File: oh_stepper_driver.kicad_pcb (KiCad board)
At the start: 2 copper layers, 61 x 43.2 mm, 26 parts, among them P1 CONN_01X04, Q1 CSD18531Q5A, Q2 CSD18531Q5A, Q3 CSD18531Q5A, Q4 CSD18531Q5A, Q5 CSD18531Q5A, Q6 CSD18531Q5A, Q7 CSD18531Q5A, Q8 CSD18531Q5A, U1 DRV8711

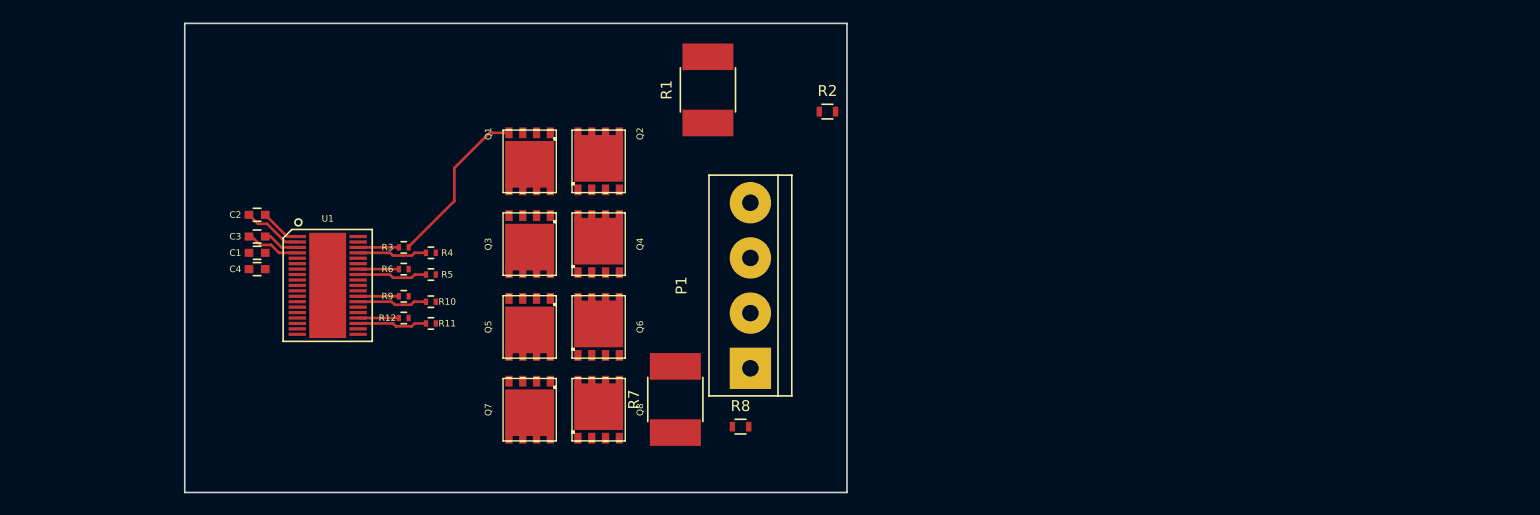
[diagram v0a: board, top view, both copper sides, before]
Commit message: FETs sheet added
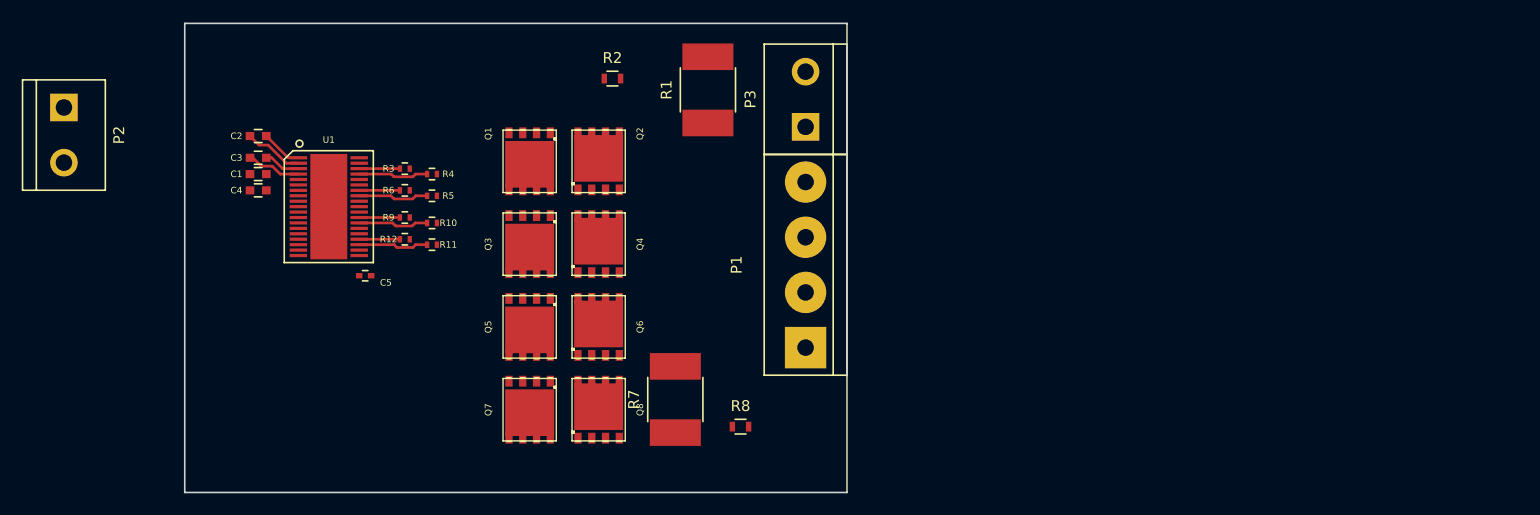
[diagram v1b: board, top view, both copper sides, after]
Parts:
- added C5: 1000pF, Capacitors_SMD:C_0402, F.Cu at (133.4, 79.1)
- added P2: CONN_01X02, Connectors:bornier2, F.Cu at (105.7, 66.2)
- added P3: CONN_01X02, Connectors:bornier2, F.Cu at (174.0, 62.9)
- moved R2 20.0 mm to (156.2, 61.0)
- moved C1 7.25 mm to (123.6, 69.8)
- moved C2 7.25 mm to (123.6, 68.2)
- moved C3 7.25 mm to (123.6, 66.2)
- moved C4 7.25 mm to (123.6, 71.2)
- moved R10 7.25 mm to (139.6, 74.2)
- moved R11 7.25 mm to (139.6, 76.2)
- moved R12 7.25 mm to (137.1, 75.8)
- moved R3 7.25 mm to (137.1, 69.2)
- moved R4 7.25 mm to (139.6, 69.8)
- moved R5 7.25 mm to (139.6, 71.8)
- moved R6 7.25 mm to (137.1, 71.2)
- moved R9 7.25 mm to (137.1, 73.8)
- moved U1 7.25 mm to (130.1, 72.8)
- moved P1 5.43 mm to (174.0, 78.1)
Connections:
- U1 pad 20: (no net) -> Net-(C5-Pad1)
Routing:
- net Net-(Q1-PadG): track 15.4 -> 0.06 mm

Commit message: adding capacitors to the PCB
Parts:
- added C7: 10uF, Capacitors_SMD:C_2220, F.Cu at (194.0, 60.8)
- added C8: 0.1uF, Capacitors_SMD:C_0603, F.Cu at (200.2, 58.7)
- added C9: 0.01uF, Capacitors_SMD:C_0603, F.Cu at (205.3, 58.7)
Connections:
- U1 pad 10: (no net) -> /STEP_AIN1
- U1 pad 11: (no net) -> /DIR_AIN2
- U1 pad 12: (no net) -> /BIN1
- U1 pad 13: (no net) -> /BIN2
- U1 pad 14: (no net) -> /SCLK
- U1 pad 15: (no net) -> /SDATI
- U1 pad 16: (no net) -> /SCS
- U1 pad 17: (no net) -> /SDATAO
- U1 pad 18: (no net) -> /FAULTn
- U1 pad 19: (no net) -> /STALLn
- U1 pad 8: (no net) -> /SLEEPn
- U1 pad 9: (no net) -> /RESET
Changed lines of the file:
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@@
 (kicad_pcb (version 20160815) (host pcbnew no-vcs-found-7399~56~ubuntu16.04.1)
   (general
-    (links 109)
-    (no_connects 97)
+    (links 113)
+    (no_connects 99)
     (area 116.764999 55.804999 177.875001 99.135001)
     (thickness 1.6)
@@
     (tracks 40)
     (zones 0)
-    (modules 29)
-    (nets 33)
+    (modules 32)
+    (nets 47)
   )
   (page A4)
@@
   (net 31 /AISENN)
   (net 32 "Net-(C5-Pad1)")
+  (net 33 /STALLn)
+  (net 34 /FAULTn)
+  (net 35 /SDATAO)
+  (net 36 /SCS)
+  (net 37 /SDATI)
+  (net 38 /SCLK)
+  (net 39 /BIN2)
+  (net 40 /BIN1)
+  (net 41 /DIR_AIN2)
+  (net 42 /STEP_AIN1)
+  (net 43 /RESET)
+  (net 44 /SLEEPn)
+  (net 45 "Net-(C7-Pad2)")
+  (net 46 "Net-(C7-Pad1)")
   (net_class Default "This is the default net class."
     (clearance 0.2)
@@
     (add_net /B2HS)
     (add_net /B2LS)
+    (add_net /BIN1)
+    (add_net /BIN2)
     (add_net /BISENN)
     (add_net /BISENP)
     (add_net /BOUT1)
     (add_net /BOUT2)
+    (add_net /DIR_AIN2)
+    (add_net /FAULTn)
+    (add_net /RESET)
+    (add_net /SCLK)
+    (add_net /SCS)
+    (add_net /SDATAO)
+    (add_net /SDATI)
+    (add_net /SLEEPn)
+    (add_net /STALLn)
+    (add_net /STEP_AIN1)
     (add_net GND)
     (add_net "Net-(C1-Pad1)")
@@
     (add_net "Net-(C4-Pad1)")
     (add_net "Net-(C5-Pad1)")
+    (add_net "Net-(C7-Pad1)")
+    (add_net "Net-(C7-Pad2)")
     (add_net "Net-(Q1-PadG)")
     (add_net "Net-(Q2-PadG)")
@@
     (add_net "Net-(Q8-PadG)")
     (add_net VM)
+  )
+  (module Capacitors_SMD:C_0603 (layer F.Cu)
+    (at 205.325119 58.662499)
+    (descr "Capacitor SMD 0603, reflow soldering, AVX (see smccp.pdf)")
+    (tags "capacitor 0603")
+    (attr smd)
+    (fp_text reference C9 (at 0 -1.9) (layer F.SilkS)
+      (effects (font (size 0.6 0.6) (thickness 0.15)))
+    )
+    (fp_text value 0.01uF (at 0 1.9) (layer F.Fab)
+      (effects (font (size 1 1) (thickness 0.15)))
+    )
+    (fp_line (start -0.8 0.4) (end -0.8 -0.4) (layer F.Fab) (width 0.15))
+    (fp_line (start 0.8 0.4) (end -0.8 0.4) (layer F.Fab) (width 0.15))
+    (fp_line (start 0.8 -0.4) (end 0.8 0.4) (layer F.Fab) (width 0.15))
+    (fp_line (start -0.8 -0.4) (end 0.8 -0.4) (layer F.Fab) (width 0.15))
+    (fp_line (start -1.45 -0.75) (end 1.45 -0.75) (layer F.CrtYd) (width 0.05))
+    (fp_line (start -1.45 0.75) (end 1.45 0.75) (layer F.CrtYd) (width 0.05))
+    (fp_line (start -1.45 -0.75) (end -1.45 0.75) (layer F.CrtYd) (width 0.05))
+    (fp_line (start 1.45 -0.75) (end 1.45 0.75) (layer F.CrtYd) (width 0.05))
+    (fp_line (start -0.35 -0.6) (end 0.35 -0.6) (layer F.SilkS) (width 0.15))
+    (fp_line (start 0.35 0.6) (end -0.35 0.6) (layer F.SilkS) (width 0.15))
+    (pad 1 smd rect (at -0.75 0) (size 0.8 0.75) (layers F.Cu F.Paste F.Mask)
+      (net 46 "Net-(C7-Pad1)"))
+    (pad 2 smd rect (at 0.75 0) (size 0.8 0.75) (layers F.Cu F.Paste F.Mask)
+      (net 45 "Net-(C7-Pad2)"))
+    (model Capacitors_SMD.3dshapes/C_0603.wrl
+      (at (xyz 0 0 0))
+      (scale (xyz 1 1 1))
+      (rotate (xyz 0 0 0))
+    )
+  )
+  (module Capacitors_SMD:C_0603 (layer F.Cu)
+    (at 200.158928 58.662499)
+    (descr "Capacitor SMD 0603, reflow soldering, AVX (see smccp.pdf)")
+    (tags "capacitor 0603")
+    (attr smd)
+    (fp_text reference C8 (at 0 -1.9) (layer F.SilkS)
+      (effects (font (size 0.6 0.6) (thickness 0.15)))
+    )
+    (fp_text value 0.1uF (at 0 1.9) (layer F.Fab)
+      (effects (font (size 1 1) (thickness 0.15)))
+    )
+    (fp_line (start 0.35 0.6) (end -0.35 0.6) (layer F.SilkS) (width 0.15))
+    (fp_line (start -0.35 -0.6) (end 0.35 -0.6) (layer F.SilkS) (width 0.15))
+    (fp_line (start 1.45 -0.75) (end 1.45 0.75) (layer F.CrtYd) (width 0.05))
+    (fp_line (start -1.45 -0.75) (end -1.45 0.75) (layer F.CrtYd) (width 0.05))
+    (fp_line (start -1.45 0.75) (end 1.45 0.75) (layer F.CrtYd) (width 0.05))
+    (fp_line (start -1.45 -0.75) (end 1.45 -0.75) (layer F.CrtYd) (width 0.05))
+    (fp_line (start -0.8 -0.4) (end 0.8 -0.4) (layer F.Fab) (width 0.15))
+    (fp_line (start 0.8 -0.4) (end 0.8 0.4) (layer F.Fab) (width 0.15))
+    (fp_line (start 0.8 0.4) (end -0.8 0.4) (layer F.Fab) (width 0.15))
+    (fp_line (start -0.8 0.4) (end -0.8 -0.4) (layer F.Fab) (width 0.15))
+    (pad 2 smd rect (at 0.75 0) (size 0.8 0.75) (layers F.Cu F.Paste F.Mask)
+      (net 45 "Net-(C7-Pad2)"))
+    (pad 1 smd rect (at -0.75 0) (size 0.8 0.75) (layers F.Cu F.Paste F.Mask)
+      (net 46 "Net-(C7-Pad1)"))
+    (model Capacitors_SMD.3dshapes/C_0603.wrl
+      (at (xyz 0 0 0))
+      (scale (xyz 1 1 1))
+      (rotate (xyz 0 0 0))
+    )
+  )
+  (module Capacitors_SMD:C_2220 (layer F.Cu)
+    (at 193.987501 60.762499)
+    (descr "Capacitor SMD 2220, reflow soldering, AVX (see smccp.pdf)")
+    (tags "capacitor 2220")
+    (attr smd)
+    (fp_text reference C7 (at 0 -4) (layer F.SilkS)
+      (effects (font (size 0.6 0.6) (thickness 0.15)))
+    )
+    (fp_text value 10uF (at 0 4) (layer F.Fab)
+      (effects (font (size 1 1) (thickness 0.15)))
+    )
+    (fp_line (start -2.3 2.725) (end 2.3 2.725) (layer F.SilkS) (width 0.15))
+    (fp_line (start 2.3 -2.725) (end -2.3 -2.725) (layer F.SilkS) (width 0.15))
+    (fp_line (start 3.6 -2.85) (end 3.6 2.85) (layer F.CrtYd) (width 0.05))
+    (fp_line (start -3.6 -2.85) (end -3.6 2.85) (layer F.CrtYd) (width 0.05))
+    (fp_line (start -3.6 2.85) (end 3.6 2.85) (layer F.CrtYd) (width 0.05))
+    (fp_line (start -3.6 -2.85) (end 3.6 -2.85) (layer F.CrtYd) (width 0.05))
+    (fp_line (start -2.75 -2.5) (end 2.75 -2.5) (layer F.Fab) (width 0.15))
+    (fp_line (start 2.75 -2.5) (end 2.75 2.5) (layer F.Fab) (width 0.15))
+    (fp_line (start 2.75 2.5) (end -2.75 2.5) (layer F.Fab) (width 0.15))
+    (fp_line (start -2.75 2.5) (end -2.75 -2.5) (layer F.Fab) (width 0.15))
+    (pad 2 smd rect (at 2.8 0) (size 1 5) (layers F.Cu F.Paste F.Mask)
+      (net 45 "Net-(C7-Pad2)"))
+    (pad 1 smd rect (at -2.8 0) (size 1 5) (layers F.Cu F.Paste F.Mask)
+      (net 46 "Net-(C7-Pad1)"))
+    (model Capacitors_SMD.3dshapes/C_2220.wrl
+      (at (xyz 0 0 0))
+      (scale (xyz 1 1 1))
+      (rotate (xyz 0 0 0))
+    )
   )
   (module Connectors:bornier2 (layer F.Cu)
@@
     (fp_line (start -5.15 3.3) (end -5.15 -4.1) (layer F.SilkS) (width 0.15))
     (fp_line (start -4.35 4.1) (end -5.15 3.3) (layer F.SilkS) (width 0.15))
-    (pad 19 smd rect (at 4.5 2.8 270) (size 0.3 1.6) (layers F.Cu F.Paste F.Mask))
+    (pad 19 smd rect (at 4.5 2.8 270) (size 0.3 1.6) (layers F.Cu F.Paste F.Mask)
+      (net 33 /STALLn))
     (pad 20 smd rect (at 4.5 -2.8 270) (size 0.3 1.6) (layers F.Cu F.Paste F.Mask)
       (net 32 "Net-(C5-Pad1)"))
-    (pad 18 smd rect (at 4 2.8 270) (size 0.3 1.6) (layers F.Cu F.Paste F.Mask))
+    (pad 18 smd rect (at 4 2.8 270) (size 0.3 1.6) (layers F.Cu F.Paste F.Mask)
+      (net 34 /FAULTn))
     (pad 21 smd rect (at 4 -2.8 270) (size 0.3 1.6) (layers F.Cu F.Paste F.Mask)
       (net 6 /BOUT2))
-    (pad 17 smd rect (at 3.5 2.8 270) (size 0.3 1.6) (layers F.Cu F.Paste F.Mask))
+    (pad 17 smd rect (at 3.5 2.8 270) (size 0.3 1.6) (layers F.Cu F.Paste F.Mask)
+      (net 35 /SDATAO))
     (pad 22 smd rect (at 3.5 -2.8 270) (size 0.3 1.6) (layers F.Cu F.Paste F.Mask)
       (net 28 /B2HS))
-    (pad 16 smd rect (at 3 2.8 270) (size 0.3 1.6) (layers F.Cu F.Paste F.Mask))
+    (pad 16 smd rect (at 3 2.8 270) (size 0.3 1.6) (layers F.Cu F.Paste F.Mask)
+      (net 36 /SCS))
     (pad 23 smd rect (at 3 -2.8 270) (size 0.3 1.6) (layers F.Cu F.Paste F.Mask)
       (net 29 /B2LS))
-    (pad 15 smd rect (at 2.5 2.8 270) (size 0.3 1.6) (layers F.Cu F.Paste F.Mask))
+    (pad 15 smd rect (at 2.5 2.8 270) (size 0.3 1.6) (layers F.Cu F.Paste F.Mask)
+      (net 37 /SDATI))
     (pad 24 smd rect (at 2.5 -2.8 270) (size 0.3 1.6) (layers F.Cu F.Paste F.Mask)
       (net 30 /BISENN))
-    (pad 14 smd rect (at 2 2.8 270) (size 0.3 1.6) (layers F.Cu F.Paste F.Mask))
+    (pad 14 smd rect (at 2 2.8 270) (size 0.3 1.6) (layers F.Cu F.Paste F.Mask)
+      (net 38 /SCLK))
     (pad 25 smd rect (at 2 -2.8 270) (size 0.3 1.6) (layers F.Cu F.Paste F.Mask)
       (net 19 /BISENP))
-    (pad 13 smd rect (at 1.5 2.8 270) (size 0.3 1.6) (layers F.Cu F.Paste F.Mask))
+    (pad 13 smd rect (at 1.5 2.8 270) (size 0.3 1.6) (layers F.Cu F.Paste F.Mask)
+      (net 39 /BIN2))
     (pad 26 smd rect (at 1.5 -2.8 270) (size 0.3 1.6) (layers F.Cu F.Paste F.Mask)
       (net 27 /B1LS))
-    (pad 12 smd rect (at 1 2.8 270) (size 0.3 1.6) (layers F.Cu F.Paste F.Mask))
+    (pad 12 smd rect (at 1 2.8 270) (size 0.3 1.6) (layers F.Cu F.Paste F.Mask)
+      (net 40 /BIN1))
     (pad 27 smd rect (at 1 -2.8 270) (size 0.3 1.6) (layers F.Cu F.Paste F.Mask)
       (net 26 /B1HS))
-    (pad 11 smd rect (at 0.5 2.8 270) (size 0.3 1.6) (layers F.Cu F.Paste F.Mask))
+    (pad 11 smd rect (at 0.5 2.8 270) (size 0.3 1.6) (layers F.Cu F.Paste F.Mask)
+      (net 41 /DIR_AIN2))
     (pad 28 smd rect (at 0.5 -2.8 270) (size 0.3 1.6) (layers F.Cu F.Paste F.Mask)
       (net 5 /BOUT1))
-    (pad 10 smd rect (at 0 2.8 270) (size 0.3 1.6) (layers F.Cu F.Paste F.Mask))
+    (pad 10 smd rect (at 0 2.8 270) (size 0.3 1.6) (layers F.Cu F.Paste F.Mask)
+      (net 42 /STEP_AIN1))
     (pad 29 smd rect (at 0 -2.8 270) (size 0.3 1.6) (layers F.Cu F.Paste F.Mask)
       (net 7 GND))
-    (pad 9 smd rect (at -0.5 2.8 270) (size 0.3 1.6) (layers F.Cu F.Paste F.Mask))
+    (pad 9 smd rect (at -0.5 2.8 270) (size 0.3 1.6) (layers F.Cu F.Paste F.Mask)
+      (net 43 /RESET))
     (pad 30 smd rect (at -0.5 -2.8 270) (size 0.3 1.6) (layers F.Cu F.Paste F.Mask)
       (net 4 /AOUT2))
-    (pad 8 smd rect (at -1 2.8 270) (size 0.3 1.6) (layers F.Cu F.Paste F.Mask))
+    (pad 8 smd rect (at -1 2.8 270) (size 0.3 1.6) (layers F.Cu F.Paste F.Mask)
+      (net 44 /SLEEPn))
     (pad 31 smd rect (at -1 -2.8 270) (size 0.3 1.6) (layers F.Cu F.Paste F.Mask)
       (net 24 /A2HS))

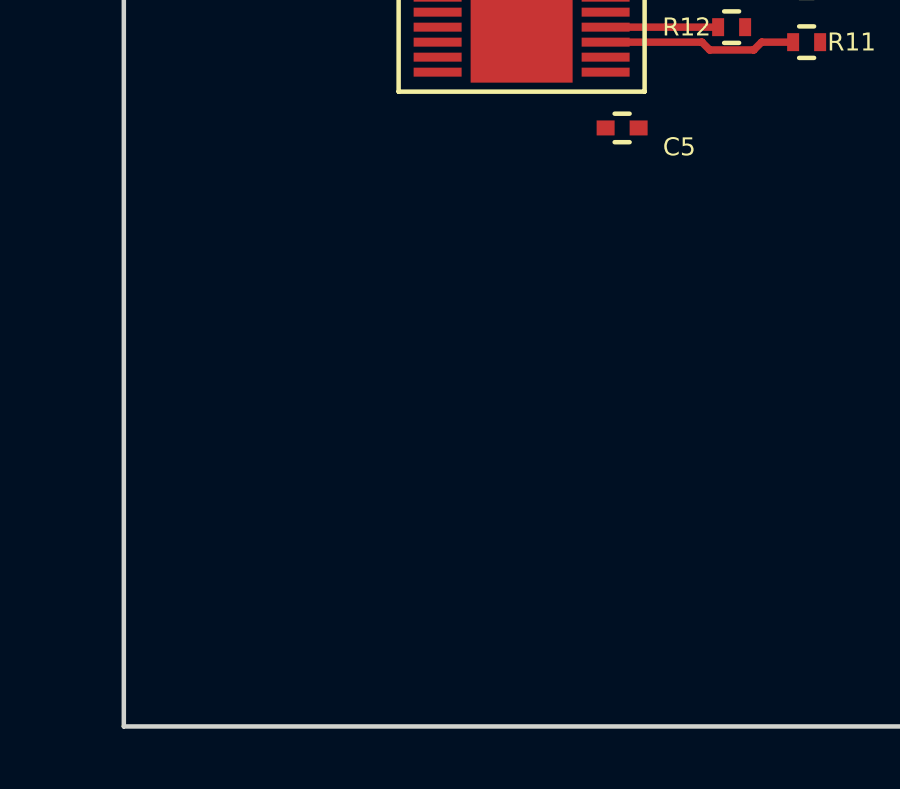
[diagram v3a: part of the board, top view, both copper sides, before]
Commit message: stm32f446 added
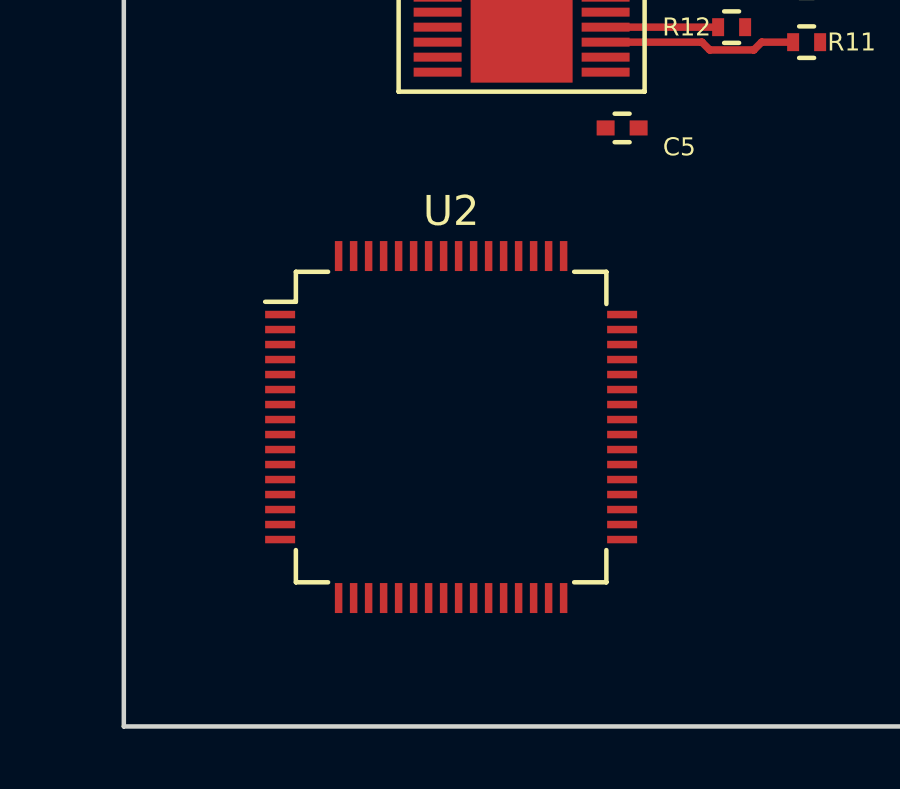
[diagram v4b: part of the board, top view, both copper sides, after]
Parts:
- added U2: STM32F446RCTx, Housings_QFP:LQFP-64_10x10mm_Pitch0.5mm, F.Cu at (127.8, 89.1)
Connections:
- net /A1HS renamed /DRV8711/A1HS
- net /A1LS renamed /DRV8711/A1LS
- net /A2HS renamed /DRV8711/A2HS
- net /A2LS renamed /DRV8711/A2LS
- net /AISENN renamed /DRV8711/AISENN
- net /AISENP renamed /DRV8711/AISENP
- net /AOUT1 renamed /DRV8711/AOUT1
- net /AOUT2 renamed /DRV8711/AOUT2
- net /B1HS renamed /DRV8711/B1HS
- net /B1LS renamed /DRV8711/B1LS
- net /B2HS renamed /DRV8711/B2HS
- net /B2LS renamed /DRV8711/B2LS
- net /BIN1 renamed /DRV8711/BIN1
- net /BIN2 renamed /DRV8711/BIN2
- net /BISENN renamed /DRV8711/BISENN
- net /BISENP renamed /DRV8711/BISENP
- net /BOUT1 renamed /DRV8711/BOUT1
- net /BOUT2 renamed /DRV8711/BOUT2
- net /DIR_AIN2 renamed /DRV8711/DIR_AIN2
- net /FAULTn renamed /DRV8711/FAULTn
- net /RESET renamed /DRV8711/RESET
- net /SCLK renamed /DRV8711/SCLK
- net /SCS renamed /DRV8711/SCS
- net /SDATAO renamed /DRV8711/SDATAO
- net /SDATI renamed /DRV8711/SDATI
- net /SLEEPn renamed /DRV8711/SLEEPn
- net /STALLn renamed /DRV8711/STALLn
- net /STEP_AIN1 renamed /DRV8711/STEP_AIN1

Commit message: connecting STM32 passives
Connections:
- net /DRV8711/BIN1 renamed /BIN1
- net /DRV8711/BIN2 renamed /BIN2
- net /DRV8711/DIR_AIN2 renamed /DIR_AIN2
- net /DRV8711/FAULTn renamed /FAULTn
- net /DRV8711/RESET renamed /RESET
- net /DRV8711/SCLK renamed /SCLK
- net /DRV8711/SCS renamed /SCS
- net /DRV8711/SDATAO renamed /SDATAO
- net /DRV8711/SDATI renamed /SDATI
- net /DRV8711/SLEEPn renamed /SLEEPn
- net /DRV8711/STALLn renamed /STALLn
- net /DRV8711/STEP_AIN1 renamed /STEP_AIN1
- net Net-(U2-Pad12) renamed GNDA
- net Net-(U2-Pad13) renamed +3.3VADC
- U2 pad 18: Net-(U2-Pad18) -> GND
- U2 pad 19: Net-(U2-Pad19) -> +3V3
- U2 pad 31: Net-(U2-Pad31) -> GND
- U2 pad 32: Net-(U2-Pad32) -> +3V3
- U2 pad 47: Net-(U2-Pad47) -> GND
- U2 pad 48: Net-(U2-Pad48) -> +3V3
- U2 pad 63: Net-(U2-Pad63) -> GND
- U2 pad 64: Net-(U2-Pad64) -> +3V3
